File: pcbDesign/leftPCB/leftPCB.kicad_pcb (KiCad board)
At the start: 2 copper layers, 57.5 x 90 mm, 22 parts, among them J1 Conn_01x12_Pin, J2 Conn_01x07_Pin, J3 Conn_01x01_Pin, J4 Conn_01x01_Pin, J5 440055-2, SW1 UP, SW2 DOWN, SW3 LEFT, SW4 RIGHT, SW5 RotaryEncoder

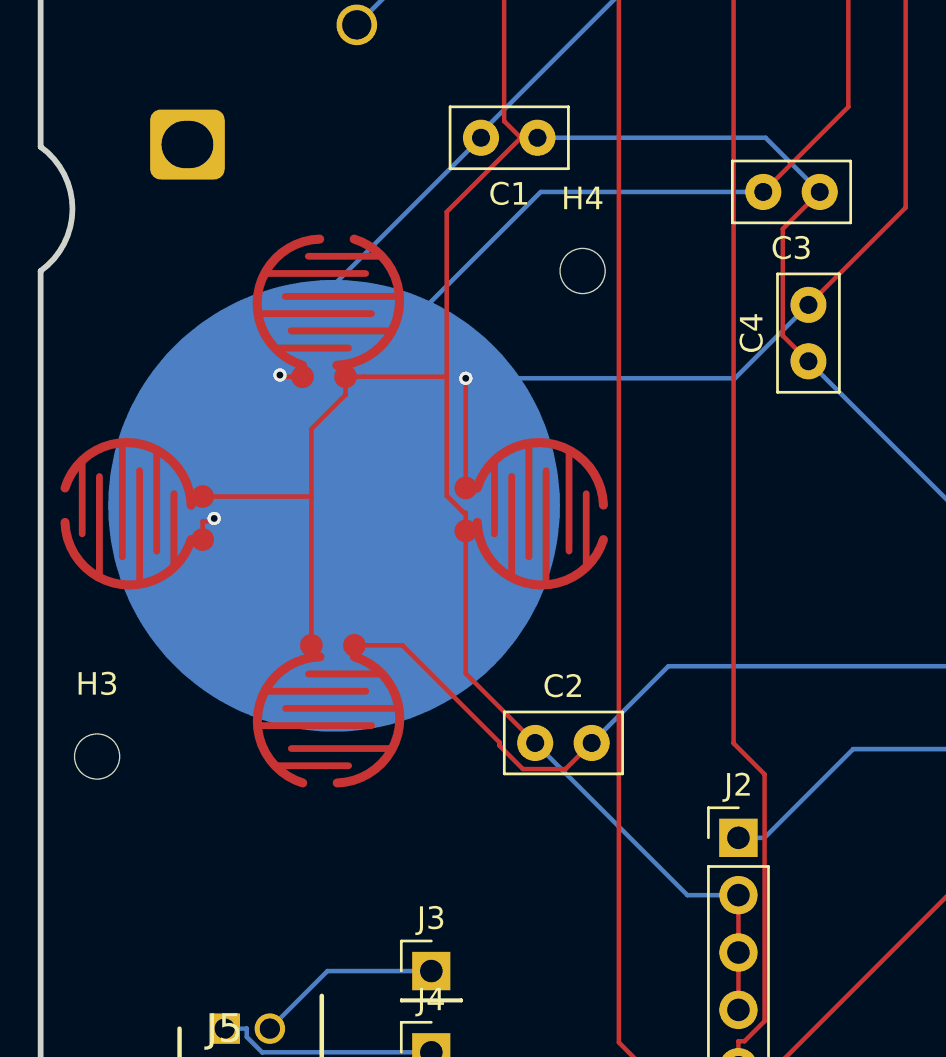
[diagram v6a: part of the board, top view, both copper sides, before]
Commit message: Fixed overlapping boards issues by cutting out areas in design Rerouted dpad traces to not interfere with each other Added "filesForOrder"
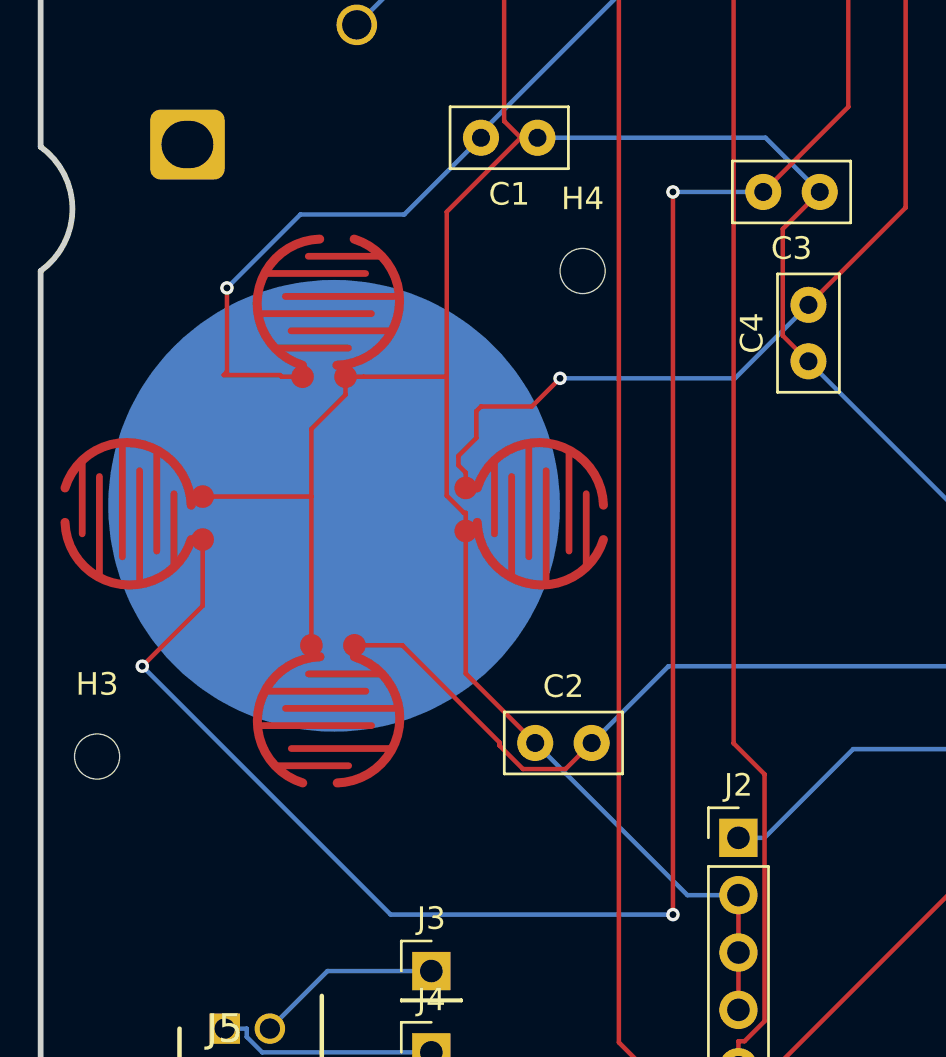
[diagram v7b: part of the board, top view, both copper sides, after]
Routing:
- net /Left: track 50.7 -> 89.8 mm, vias 1 -> 3
- net /Up: track 36.0 -> 42.2 mm
- net /Right: track 45.7 -> 44.8 mm
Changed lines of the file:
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@@
 	)
 	(segment
-		(start 133.597 76.183)
-		(end 132.7953 76.183)
-		(width 0.2)
-		(layer "F.Cu")
-		(net 3)
-	)
-	(segment
-		(start 132.7953 76.183)
+		(start 130.25 72.25)
+		(end 130.25 75.9668)
+		(width 0.2)
+		(layer "F.Cu")
+		(net 3)
+	)
+	(segment
+		(start 130.25 75.9668)
+		(end 130.1084 76.1084)
+		(width 0.2)
+		(layer "F.Cu")
+		(net 3)
+	)
+	(segment
+		(start 130.1084 76.1084)
+		(end 132.5948 76.1084)
+		(width 0.2)
+		(layer "F.Cu")
+		(net 3)
+	)
+	(segment
+		(start 132.5948 76.1084)
 		(end 132.6694 76.183)
 		(width 0.2)
@@
 	(segment
 		(start 132.6694 76.183)
-		(end 132.5948 76.1084)
+		(end 133.597 76.183)
 		(width 0.2)
 		(layer "F.Cu")
@@
 	)
 	(via
-		(at 132.5948 76.1084)
+		(at 130.25 72.25)
 		(size 0.6)
 		(drill 0.3)
@@
 	)
 	(segment
-		(start 132.5948 74.5052)
-		(end 132.5948 76.1084)
+		(start 133.5 69)
+		(end 130.25 72.25)
 		(width 0.2)
 		(layer "B.Cu")
@@
 	)
 	(segment
+		(start 141.5 65.6)
+		(end 138.1 69)
+		(width 0.2)
+		(layer "B.Cu")
+		(net 3)
+	)
+	(segment
+		(start 138.1 69)
+		(end 133.5 69)
+		(width 0.2)
+		(layer "B.Cu")
+		(net 3)
+	)
+	(segment
 		(start 141.5 65.3767)
 		(end 141.5 65.6)
-		(width 0.2)
-		(layer "B.Cu")
-		(net 3)
-	)
-	(segment
-		(start 141.5 65.6)
-		(end 132.5948 74.5052)
 		(width 0.2)
 		(layer "B.Cu")
@@
 	)
 	(segment
+		(start 143.7529 77.5)
+		(end 145 76.2529)
+		(width 0.2)
+		(layer "F.Cu")
+		(net 9)
+	)
+	(segment
+		(start 140.5 80.1013)
+		(end 140.5 79.690964)
+		(width 0.2)
+		(layer "F.Cu")
+		(net 9)
+	)
+	(segment
+		(start 140.5 79.690964)
+		(end 141.291964 78.899)
+		(width 0.2)
+		(layer "F.Cu")
+		(net 9)
+	)
+	(segment
+		(start 140.8258 81.1081)
+		(end 140.8258 80.4271)
+		(width 0.2)
+		(layer "F.Cu")
+		(net 9)
+	)
+	(segment
 		(start 160.305 68.695)
 		(end 156 73)
@@
 	)
 	(segment
+		(start 141.291964 77.708036)
+		(end 141.5 77.5)
+		(width 0.2)
+		(layer "F.Cu")
+		(net 9)
+	)
+	(segment
+		(start 140.8258 80.4271)
+		(end 140.5 80.1013)
+		(width 0.2)
+		(layer "F.Cu")
+		(net 9)
+	)
+	(segment
 		(start 160.305 50.5)
 		(end 160.305 68.695)
@@
 	)
 	(segment
-		(start 140.8258 81.1081)
-		(end 140.8258 76.2529)
+		(start 141.5 77.5)
+		(end 143.7529 77.5)
+		(width 0.2)
+		(layer "F.Cu")
+		(net 9)
+	)
+	(segment
+		(start 141.291964 78.899)
+		(end 141.291964 77.708036)
 		(width 0.2)
 		(layer "F.Cu")
@@
 	)
 	(via
-		(at 140.8258 76.2529)
+		(at 145 76.2529)
 		(size 0.6)
 		(drill 0.3)
@@
 	)
 	(segment
-		(start 156 73)
+		(start 152.7471 76.2529)
+		(end 156 73)
+		(width 0.2)
+		(layer "B.Cu")
+		(net 9)
+	)
+	(segment
+		(start 145 76.2529)
 		(end 152.7471 76.2529)
 		(width 0.2)
 		(layer "B.Cu")
 		(net 9)
-	)
-	(segment
-		(start 152.7471 76.2529)
-		(end 140.8258 76.2529)
-		(width 0.2)
-		(layer "B.Cu")
-		(net 9)
-	)
-	(segment
-		(start 129.1749 83.3941)
-		(end 129.1749 82.5924)
-		(width 0.2)
-		(layer "F.Cu")
-		(net 10)
 	)
 	(segment
@@
 	)
 	(segment
-		(start 129.551 82.5924)
-		(end 129.1749 82.5924)
-		(width 0.2)
-		(layer "F.Cu")
-		(net 10)
-	)
-	(segment
-		(start 129.6854 82.458)
-		(end 129.551 82.5924)
+		(start 150 68)
+		(end 150 100)
+		(width 0.2)
+		(layer "F.Cu")
+		(net 10)
+	)
+	(segment
+		(start 126.5 89)
+		(end 129.1749 86.3251)
+		(width 0.2)
+		(layer "F.Cu")
+		(net 10)
+	)
+	(segment
+		(start 129.1749 86.3251)
+		(end 129.1749 83.3941)
 		(width 0.2)
 		(layer "F.Cu")
@@
 	)
 	(via
-		(at 129.6854 82.458)
+		(at 150 100)
 		(size 0.6)
 		(drill 0.3)
@@
 		(net 10)
 	)
-	(segment
-		(start 144.1434 68)
-		(end 129.6854 82.458)
+	(via
+		(at 150 68)
+		(size 0.6)
+		(drill 0.3)
+		(layers "F.Cu" "B.Cu")
+		(net 10)
+	)
+	(via
+		(at 126.5 89)
+		(size 0.6)
+		(drill 0.3)
+		(layers "F.Cu" "B.Cu")
+		(net 10)
+	)
+	(segment
+		(start 150 100)
+		(end 137.5 100)
+		(width 0.2)
+		(layer "B.Cu")
+		(net 10)
+	)
+	(segment
+		(start 137.5 100)
+		(end 126.5 89)
 		(width 0.2)
 		(layer "B.Cu")
@@
 	(segment
 		(start 154 68)
-		(end 144.1434 68)
-		(width 0.2)
-		(layer "B.Cu")
+		(end 150 68)
+		(width 0.2)
+		(layer "B.Cu")
